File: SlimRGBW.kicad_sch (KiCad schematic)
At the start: 9 parts, among them J1 Programming, J2 Power, U1 ESP32-C3-MINI-1

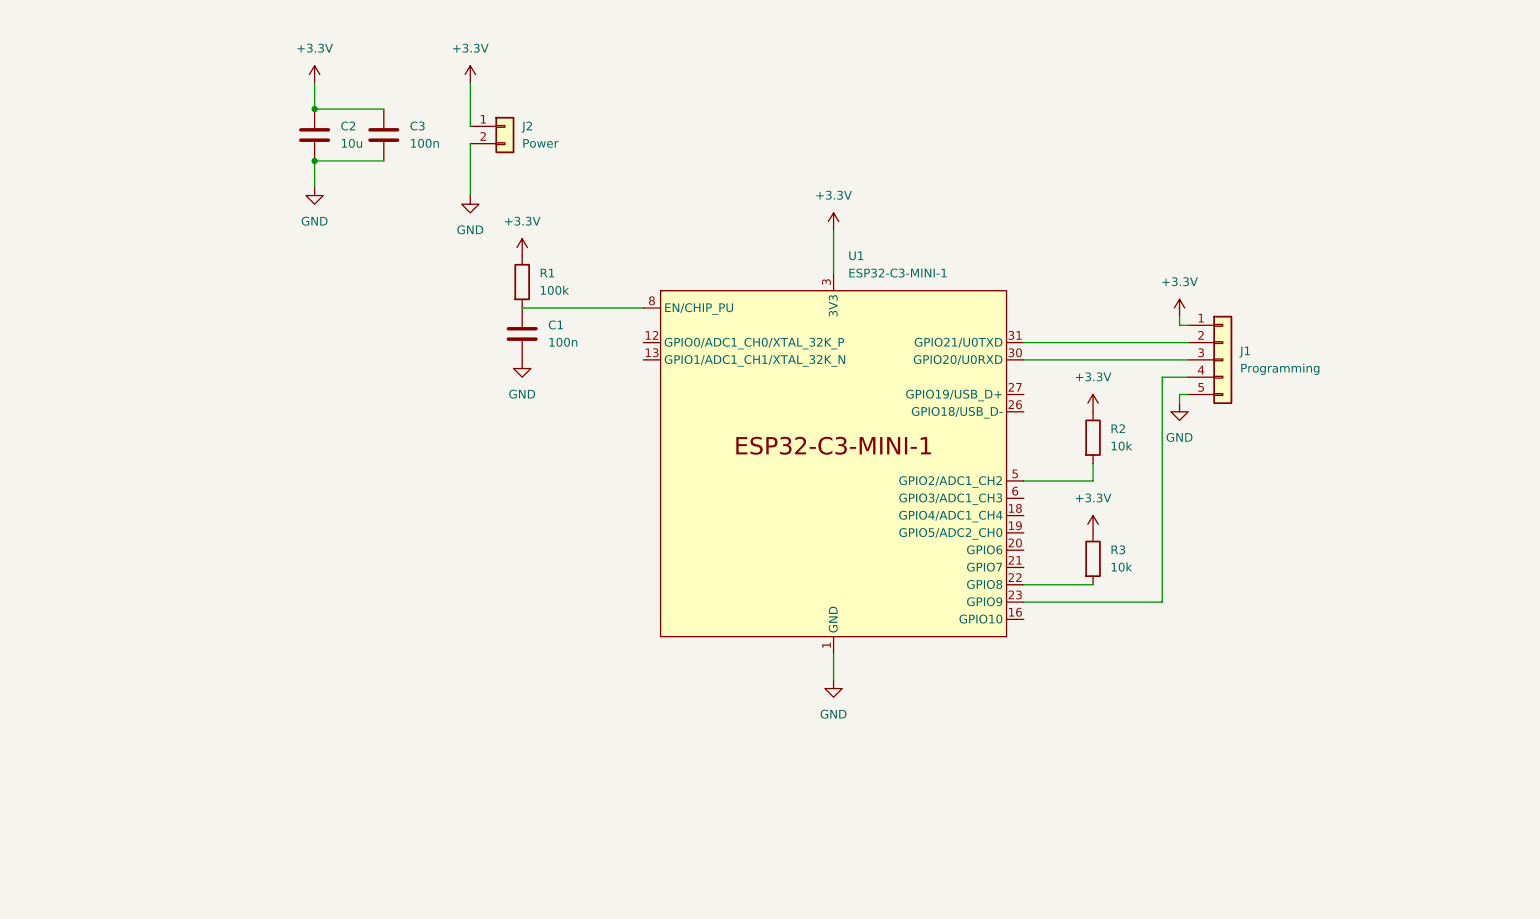
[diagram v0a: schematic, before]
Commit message: Add mosfets to schematic, no footprint yet
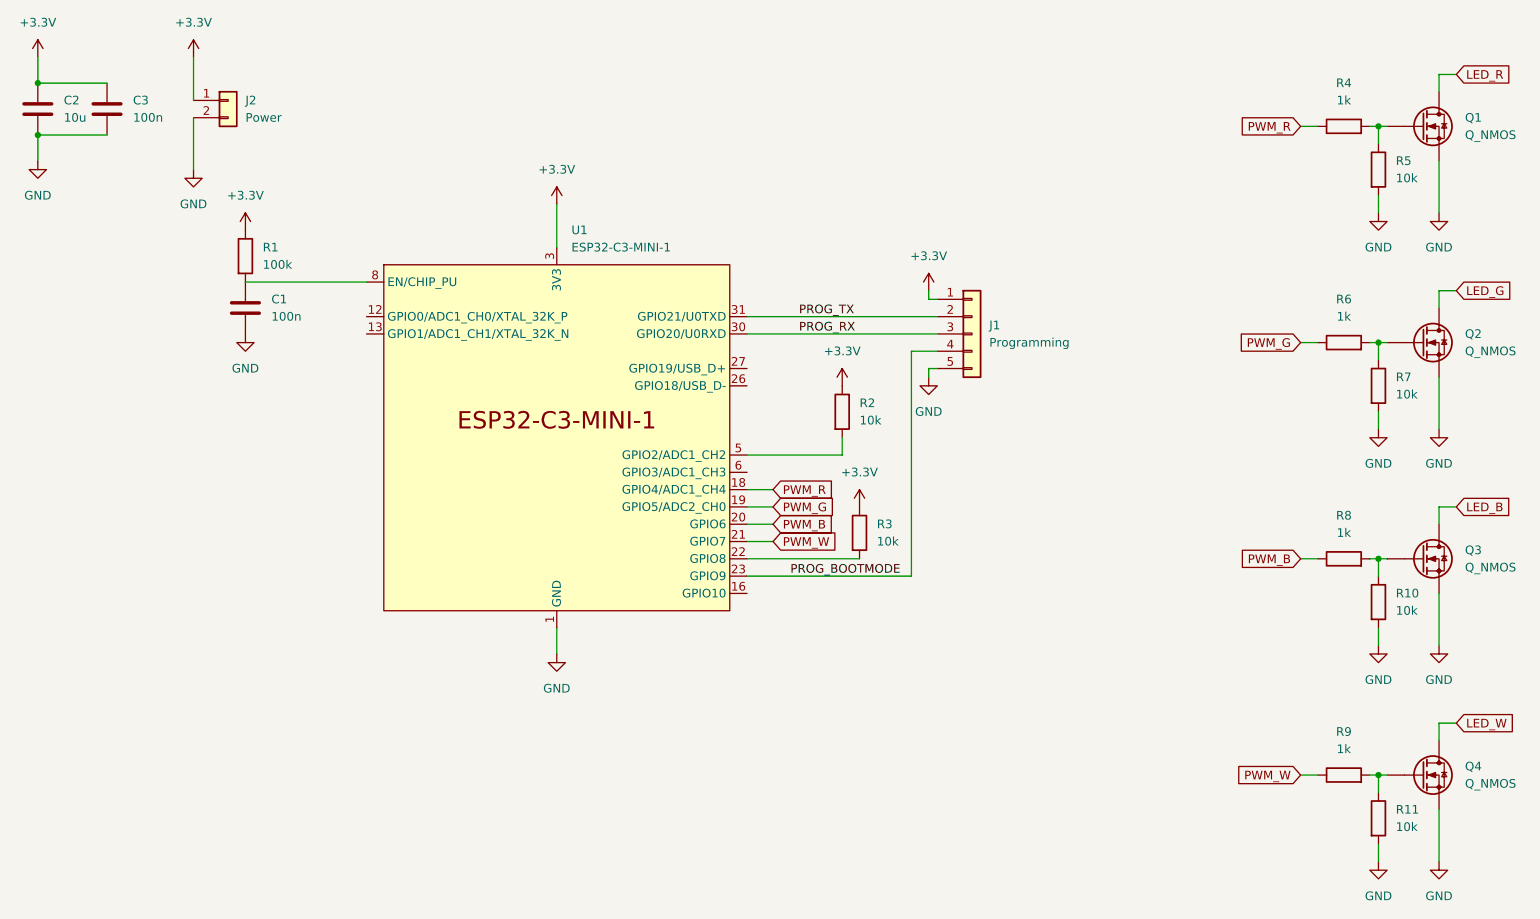
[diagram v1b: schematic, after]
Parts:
- added Q1, Q2, Q3, Q4: Q_NMOS, symbol Device:Q_NMOS
- added R10, R11, R5, R7: 10k, Resistor_SMD:R_0402_1005Metric, symbol Device:R
- added R4, R6, R8, R9: 1k, Resistor_SMD:R_0402_1005Metric, symbol Device:R
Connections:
- net GND: now also Q1.S, Q2.S, Q3.S, Q4.S, R10.2, R11.2, R5.2, R7.2
- net PROG_TX: now reaches J1.2 (Pin_2), U1.31 (GPIO21/U0TXD)
- net PROG_RX: now reaches J1.3 (Pin_3), U1.30 (GPIO20/U0RXD)
- net PROG_BOOTMODE: now reaches J1.4 (Pin_4), U1.23 (GPIO9)
- net PWM_R: now reaches U1.18 (GPIO4/ADC1_CH4)
- net PWM_R: now also R4.1
- net PWM_G: now reaches U1.19 (GPIO5/ADC2_CH0)
- net PWM_G: now also R6.1
- net PWM_B: now reaches U1.20 (GPIO6)
- net PWM_B: now also R8.1
- net PWM_W: now reaches U1.21 (GPIO7)
- net PWM_W: now also R9.1
- new net: Q3.G, R10.1, R8.2
- new net: Q1.G, R4.2, R5.1
- new net: Q2.G, R6.2, R7.1
- new net: Q4.G, R11.1, R9.2
- new net LED_B: Q3.D
- new net LED_G: Q2.D
- new net LED_R: Q1.D
- new net LED_W: Q4.D
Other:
- moved on the sheet: C1, C2, C3, J1, J2, R1, R2, R3, U1
